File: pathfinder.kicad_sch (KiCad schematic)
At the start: 2 parts, among them SW1 SW_Push, U1 XIAO-RP2040-DIP

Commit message: dump
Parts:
- added D1, D2, D3: L08R5000Q1, L08R5000Q1:LEDRD254W57D500H1070, symbol L08R5000Q1:L08R5000Q1
- added R1, R2, R3: R, symbol Device:R
- added SW2, SW3: SW_Push, symbol Switch:SW_Push
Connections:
- net button1: now reaches SW1.1
- net button1: now also U1.1 (P26_A0_D0)
- net GND: now reaches SW1.2
- net GND: now also U1.13 (GND), D1.C, D2.C, D3.C, SW2.2, SW3.2
- net button2: now reaches U1.2 (P27_A1_D1)
- net button2: now also SW2.1
- net button3: now reaches U1.3 (P28_A2_D2)
- net button3: now also SW3.1
- net LED1: now reaches U1.4 (P29_A3_D3)
- net LED1: now also R1.2
- net LED2: now reaches U1.5 (P6_SDA_D4)
- net LED2: now also R2.2
- net LED3: now reaches U1.6 (P7_SCL_D5)
- net LED3: now also R3.2
- new net: D2.A, R2.1
- new net: D3.A, R3.1
- new net: D1.A, R1.1
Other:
- moved on the sheet: SW1, U1

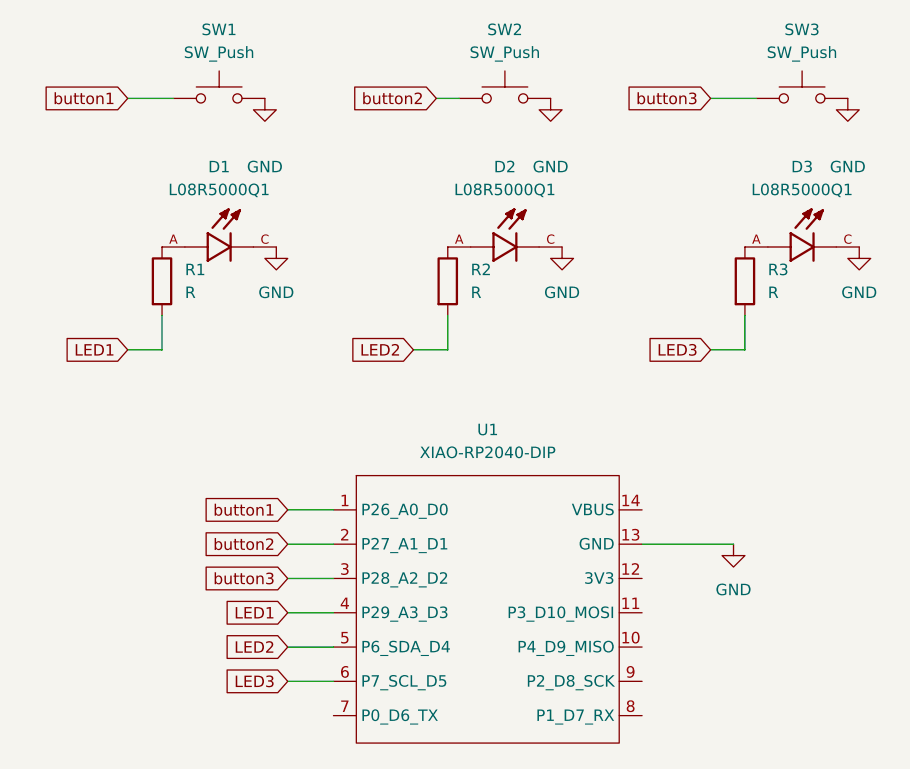
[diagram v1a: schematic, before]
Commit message: installing a buzer in the schematic desgin
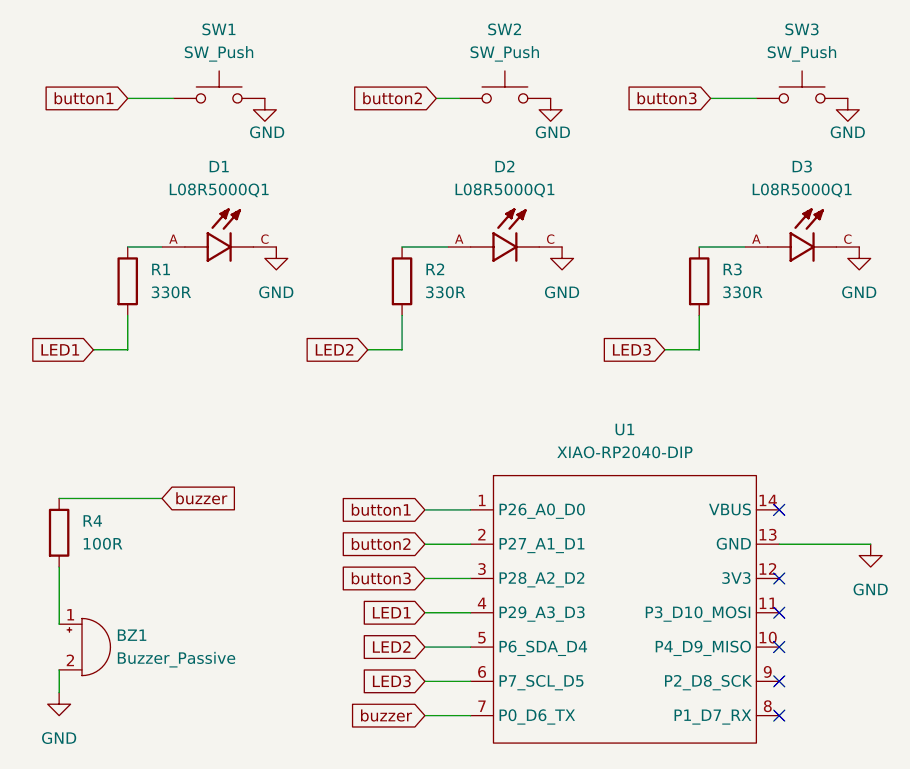
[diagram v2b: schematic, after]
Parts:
- added BZ1: Buzzer_Passive, Buzzer_Beeper:Buzzer_12x9.5RM7.6, symbol Device:Buzzer
- added R4: 100R, symbol Device:R
- R1, R2, R3: value R -> 330R
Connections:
- net GND: now also BZ1.2 (-)
- net buzzer: now reaches U1.7 (P0_D6_TX)
- net buzzer: now also R4.1
- new net: BZ1.1 (+), R4.2
- no-connect marks 0 -> 6
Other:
- moved on the sheet: R1, R2, R3, U1

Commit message: mapped footprints & added all the 3d files
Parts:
- R1, R2, R3, R4: footprint (none) -> Resistor_THT:R_Axial_DIN0204_L3.6mm_D1.6mm_P5.08mm_Horizontal
- SW1, SW2, SW3: footprint (none) -> Button_Switch_Keyboard:SW_Cherry_MX_1.00u_PCB
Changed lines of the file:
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@@
 			)
 		)
-		(property "Footprint" ""
+		(property "Footprint" "Button_Switch_Keyboard:SW_Cherry_MX_1.00u_PCB"
 			(at 104.14 54.61 0)
 			(hide yes)
@@
 			)
 		)
-		(property "Footprint" ""
+		(property "Footprint" "Resistor_THT:R_Axial_DIN0204_L3.6mm_D1.6mm_P5.08mm_Horizontal"
 			(at 92.202 80.01 90)
 			(hide yes)
@@
 			)
 		)
-		(property "Footprint" ""
+		(property "Footprint" "Button_Switch_Keyboard:SW_Cherry_MX_1.00u_PCB"
 			(at 168.91 54.61 0)
 			(hide yes)
@@
 			)
 		)
-		(property "Footprint" ""
+		(property "Footprint" "Resistor_THT:R_Axial_DIN0204_L3.6mm_D1.6mm_P5.08mm_Horizontal"
 			(at 86.36 107.95 90)
 			(hide yes)
@@
 			)
 		)
-		(property "Footprint" ""
+		(property "Footprint" "Resistor_THT:R_Axial_DIN0204_L3.6mm_D1.6mm_P5.08mm_Horizontal"
 			(at 155.702 80.01 90)
 			(hide yes)
@@
 			)
 		)
-		(property "Footprint" ""
+		(property "Footprint" "Button_Switch_Keyboard:SW_Cherry_MX_1.00u_PCB"
 			(at 135.89 54.61 0)
 			(hide yes)
@@
 			)
 		)
-		(property "Footprint" ""
+		(property "Footprint" "Resistor_THT:R_Axial_DIN0204_L3.6mm_D1.6mm_P5.08mm_Horizontal"
 			(at 122.682 80.01 90)
 			(hide yes)

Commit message: added a BOM, done some final changes & added a README file
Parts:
- R1, R2, R3, R4: footprint Resistor_THT:R_Axial_DIN0204_L3.6mm_D1.6mm_P5.08mm_Horizontal -> Resistor_THT:R_Axial_DIN0411_L9.9mm_D3.6mm_P12.70mm_Horizontal
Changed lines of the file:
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@@
 			)
 		)
-		(property "Footprint" "Resistor_THT:R_Axial_DIN0204_L3.6mm_D1.6mm_P5.08mm_Horizontal"
+		(property "Footprint" "Resistor_THT:R_Axial_DIN0411_L9.9mm_D3.6mm_P12.70mm_Horizontal"
 			(at 92.202 80.01 90)
 			(hide yes)
@@
 			)
 		)
-		(property "Footprint" "Resistor_THT:R_Axial_DIN0204_L3.6mm_D1.6mm_P5.08mm_Horizontal"
+		(property "Footprint" "Resistor_THT:R_Axial_DIN0411_L9.9mm_D3.6mm_P12.70mm_Horizontal"
 			(at 86.36 107.95 90)
 			(hide yes)
@@
 			)
 		)
-		(property "Footprint" "Resistor_THT:R_Axial_DIN0204_L3.6mm_D1.6mm_P5.08mm_Horizontal"
+		(property "Footprint" "Resistor_THT:R_Axial_DIN0411_L9.9mm_D3.6mm_P12.70mm_Horizontal"
 			(at 155.702 80.01 90)
 			(hide yes)
@@
 			)
 		)
-		(property "Footprint" "Resistor_THT:R_Axial_DIN0204_L3.6mm_D1.6mm_P5.08mm_Horizontal"
+		(property "Footprint" "Resistor_THT:R_Axial_DIN0411_L9.9mm_D3.6mm_P12.70mm_Horizontal"
 			(at 122.682 80.01 90)
 			(hide yes)
